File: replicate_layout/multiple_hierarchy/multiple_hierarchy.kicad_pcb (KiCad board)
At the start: 2 copper layers, 72 parts, among them J1001 Pusa_4mm, J1002 Pusa_4mm, J201 Pusa_4mm, J202 Pusa_4mm, J601 Pusa_4mm, J602 Pusa_4mm, Q1101 CSD19531KCS, Q1102 CSD19531KCS, Q1301 CSD19531KCS, Q1302 CSD19531KCS, Q1401 CSD19531KCS, Q1402 CSD19531KCS, Q301 CSD19531KCS, Q302 CSD19531KCS, Q501 CSD19531KCS, Q502 CSD19531KCS, Q701 CSD19531KCS, Q702 CSD19531KCS, Q901 CSD19531KCS, Q902 CSD19531KCS, U101 TMS320F28027DA, U1101 IR2181, U1201 INA240, U1301 IR2181, U1401 IR2181, U301 IR2181, U401 INA240, U501 IR2181, U701 IR2181, U801 INA240, U901 IR2181

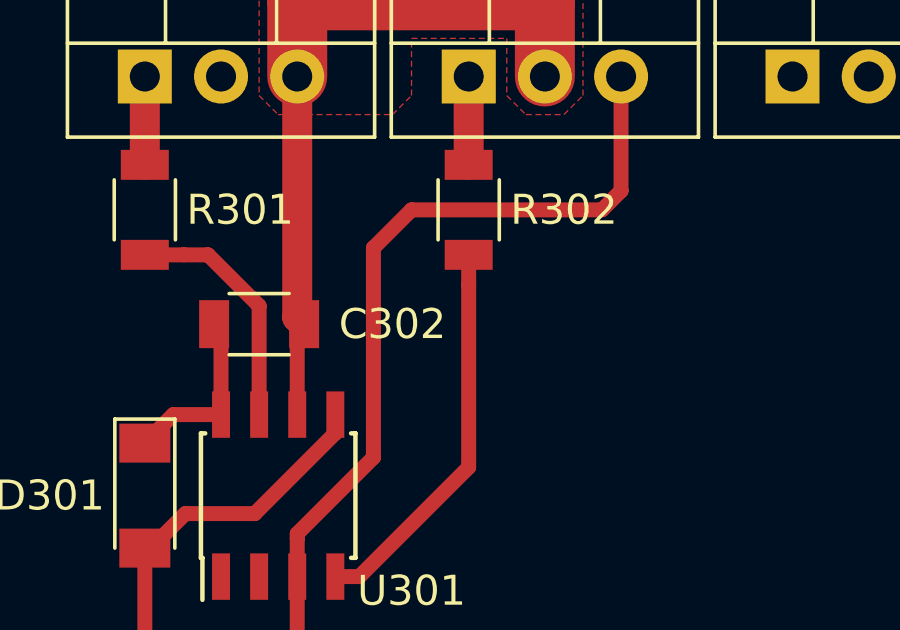
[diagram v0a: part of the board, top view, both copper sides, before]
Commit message: replicate all drawings
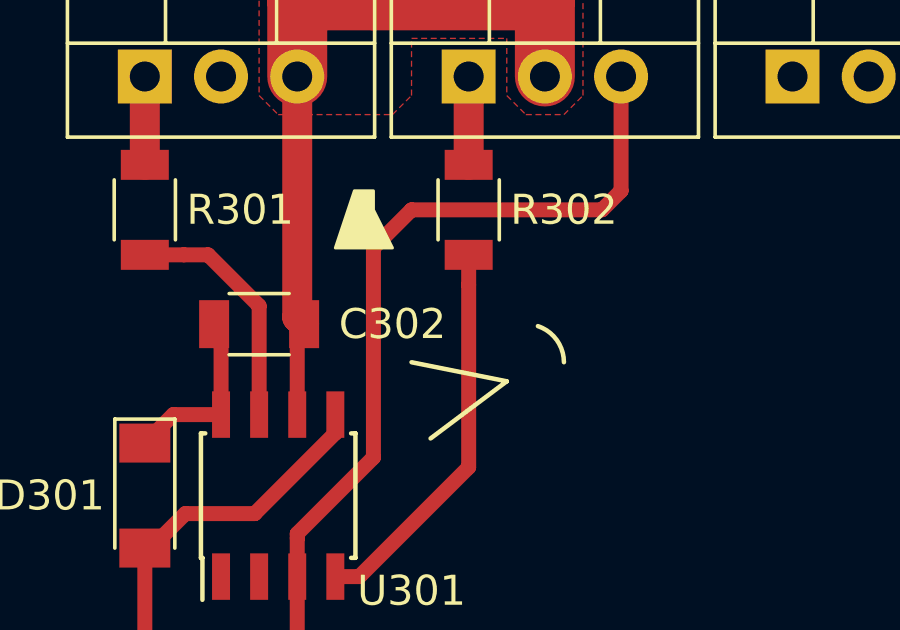
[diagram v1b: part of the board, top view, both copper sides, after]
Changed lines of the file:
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@@
-(kicad_pcb (version 20171130) (host pcbnew "(6.0.0-rc1-dev-1691-g44cb979e9)")
+(kicad_pcb (version 20171130) (host pcbnew "(5.1.0)-1")
   (general
     (thickness 1.6)
-    (drawings 1)
+    (drawings 8)
     (tracks 89)
     (zones 0)
@@
     )
   )
+  (gr_poly (pts (xy 92.71 57.15) (xy 92.075 59.055) (xy 93.98 59.055) (xy 93.345 57.785) (xy 93.345 57.15)) (layer F.SilkS) (width 0.1))
+  (gr_arc (start 98.425 62.865) (end 99.695 62.865) (angle -71.56505118) (layer F.SilkS) (width 0.15))
+  (gr_circle (center 99.695 59.055) (end 100.33 59.69) (layer F.Fab) (width 0.15))
+  (gr_line (start 97.79 63.5) (end 95.25 65.405) (layer F.SilkS) (width 0.15))
+  (gr_line (start 97.79 63.5) (end 94.615 62.865) (layer F.SilkS) (width 0.15))
+  (gr_line (start 98.425 61.595) (end 99.06 63.5) (layer F.Fab) (width 0.15))
+  (gr_line (start 94.615 63.5) (end 98.425 61.595) (layer F.Fab) (width 0.15))
   (gr_text A (at 98.425 66.675 90) (layer F.Fab)
     (effects (font (size 3 3) (thickness 0.5)))
@@
       )
     )
+  )
+  (zone (net 0) (net_name "") (layer F.Cu) (hatch edge 0.508)
+    (connect_pads (clearance 0.508))
+    (min_thickness 0.254)
+    (keepout (tracks not_allowed) (vias not_allowed) (copperpour not_allowed))
+    (fill (arc_segments 32) (thermal_gap 0.508) (thermal_bridge_width 0.508))
+    (polygon
+      (pts
+        (xy 87.63 56.515) (xy 89.535 56.515) (xy 89.535 58.42) (xy 87.63 58.42)
+      )
+    )

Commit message: Updated test projects
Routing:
- net -VDC: track 66.1 -> 66.2 mm, vias 0 -> 2
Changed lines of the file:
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@@
-(kicad_pcb (version 20171130) (host pcbnew "(5.1.0)-1")
+(kicad_pcb (version 20171130) (host pcbnew "(5.1.2)-1")
   (general
     (thickness 1.6)
     (drawings 8)
-    (tracks 89)
+    (tracks 95)
     (zones 0)
     (modules 72)
@@
   )
   (setup
-    (last_trace_width 0.25)
+    (last_trace_width 0.4)
     (user_trace_width 0.4)
     (user_trace_width 0.5)
@@
   (segment (start 90.805 68.735) (end 90.805 70.01) (width 0.5) (layer F.Cu) (net 14))
   (segment (start 90.805 68.58) (end 90.805 68.735) (width 0.5) (layer F.Cu) (net 14))
-  (segment (start 93.345 59.055) (end 93.345 66.04) (width 0.5) (layer F.Cu) (net 14))
   (segment (start 93.345 66.04) (end 90.805 68.58) (width 0.5) (layer F.Cu) (net 14))
   (segment (start 90.805 72.62) (end 90.4 73.025) (width 0.5) (layer F.Cu) (net 14))
@@
   (segment (start 186.055 54.135) (end 186.055 53.66) (width 0.5) (layer F.Cu) (net 14))
   (segment (start 186.055 53.66) (end 185.255 52.86) (width 0.5) (layer F.Cu) (net 14))
+  (via (at 93.472 65.024) (size 0.8) (drill 0.4) (layers F.Cu B.Cu) (net 14))
+  (segment (start 93.345 66.04) (end 93.345 65.151) (width 0.4) (layer F.Cu) (net 14))
+  (segment (start 93.345 65.151) (end 93.472 65.024) (width 0.4) (layer F.Cu) (net 14))
+  (segment (start 93.472 65.024) (end 93.472 60.452) (width 0.4) (layer B.Cu) (net 14))
+  (via (at 93.472 60.452) (size 0.8) (drill 0.4) (layers F.Cu B.Cu) (net 14))
+  (segment (start 93.472 59.182) (end 93.472 60.452) (width 0.4) (layer F.Cu) (net 14))
+  (segment (start 93.345 59.055) (end 93.472 59.182) (width 0.4) (layer F.Cu) (net 14))
   (segment (start 87.025 59.285) (end 85.725 59.285) (width 0.5) (layer F.Cu) (net 17))
   (segment (start 87.835002 59.285) (end 87.025 59.285) (width 0.5) (layer F.Cu) (net 17))

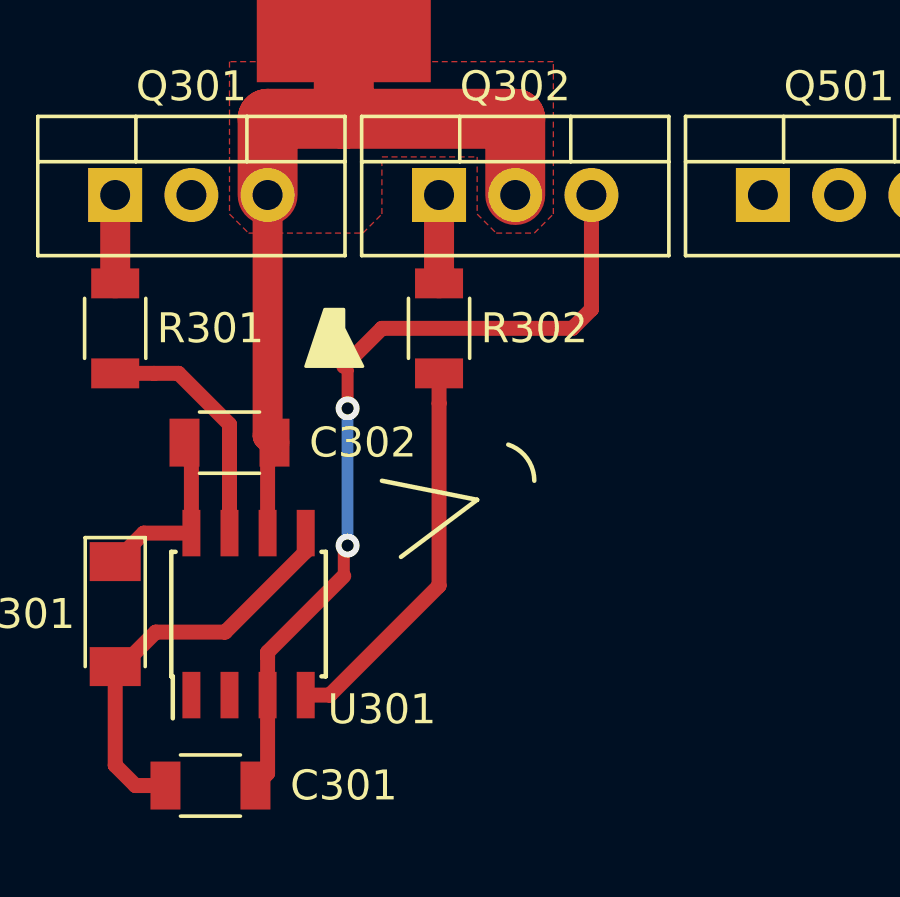
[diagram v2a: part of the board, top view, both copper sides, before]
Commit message: Modified test layouts so that one footprint is on bottom layer
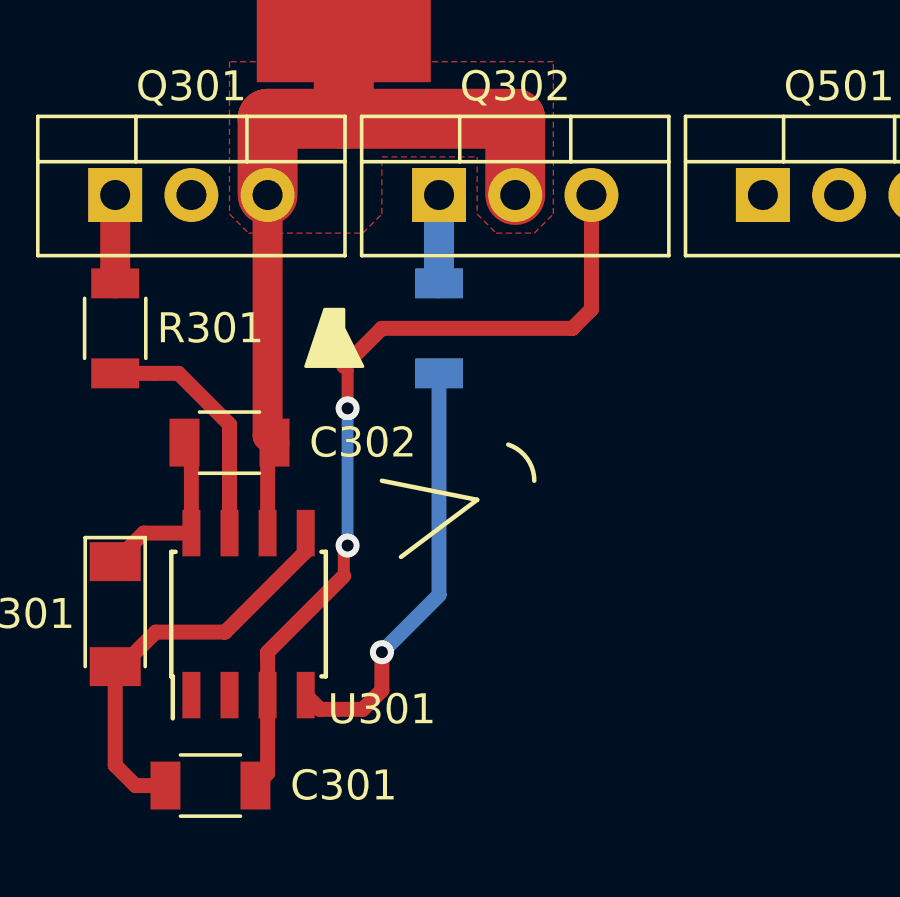
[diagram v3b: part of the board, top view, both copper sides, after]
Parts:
- R302: moved to B.Cu
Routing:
- net Net-(R302-Pad1): track 13.0 -> 14.4 mm, vias 0 -> 1
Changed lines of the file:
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@@
-(kicad_pcb (version 20171130) (host pcbnew "(5.1.2)-1")
+(kicad_pcb (version 20171130) (host pcbnew "(5.1.5-90-g5c7ac1bb7)-1")
   (general
     (thickness 1.6)
     (drawings 8)
-    (tracks 95)
+    (tracks 98)
     (zones 0)
     (modules 72)
@@
   )
   (setup
-    (last_trace_width 0.4)
+    (last_trace_width 0.5)
     (user_trace_width 0.4)
     (user_trace_width 0.5)
@@
     )
   )
-  (module Passives:R1206M (layer F.Cu)
+  (module Passives:R1206M (layer B.Cu)
     (at 96.52 57.785 90)
     (descr "Capacitor SMD 1206, reflow soldering, AVX (see smccp.pdf)")
     (tags "capacitor 1206")
     (attr smd)
-    (fp_text reference R302 (at 0 3.175 180) (layer F.SilkS)
-      (effects (font (size 1 1) (thickness 0.15)))
+    (fp_text reference R302 (at 0 -3.175 180) (layer B.SilkS)
+      (effects (font (size 1 1) (thickness 0.15)) (justify mirror))
     )
-    (fp_text value 22R (at 0 2 90) (layer F.Fab) hide
-      (effects (font (size 1 1) (thickness 0.15)))
+    (fp_text value 22R (at 0 -2 270) (layer B.Fab) hide
+      (effects (font (size 1 1) (thickness 0.15)) (justify mirror))
     )
-    (fp_line (start 2.25 1.05) (end -2.25 1.05) (layer F.CrtYd) (width 0.05))
-    (fp_line (start 2.25 1.05) (end 2.25 -1.05) (layer F.CrtYd) (width 0.05))
-    (fp_line (start -2.25 -1.05) (end -2.25 1.05) (layer F.CrtYd) (width 0.05))
-    (fp_line (start -2.25 -1.05) (end 2.25 -1.05) (layer F.CrtYd) (width 0.05))
-    (fp_line (start -1 1.02) (end 1 1.02) (layer F.SilkS) (width 0.12))
-    (fp_line (start 1 -1.02) (end -1 -1.02) (layer F.SilkS) (width 0.12))
-    (fp_line (start -1.6 -0.8) (end 1.6 -0.8) (layer F.Fab) (width 0.1))
-    (fp_line (start 1.6 -0.8) (end 1.6 0.8) (layer F.Fab) (width 0.1))
-    (fp_line (start 1.6 0.8) (end -1.6 0.8) (layer F.Fab) (width 0.1))
-    (fp_line (start -1.6 0.8) (end -1.6 -0.8) (layer F.Fab) (width 0.1))
-    (fp_text user %R (at 0 0 90) (layer F.Fab)
-      (effects (font (size 0.5 0.5) (thickness 0.07)))
+    (fp_line (start 2.25 -1.05) (end -2.25 -1.05) (layer B.CrtYd) (width 0.05))
+    (fp_line (start 2.25 -1.05) (end 2.25 1.05) (layer B.CrtYd) (width 0.05))
+    (fp_line (start -2.25 1.05) (end -2.25 -1.05) (layer B.CrtYd) (width 0.05))
+    (fp_line (start -2.25 1.05) (end 2.25 1.05) (layer B.CrtYd) (width 0.05))
+    (fp_line (start -1 -1.02) (end 1 -1.02) (layer B.SilkS) (width 0.12))
+    (fp_line (start 1 1.02) (end -1 1.02) (layer B.SilkS) (width 0.12))
+    (fp_line (start -1.6 0.8) (end 1.6 0.8) (layer B.Fab) (width 0.1))
+    (fp_line (start 1.6 0.8) (end 1.6 -0.8) (layer B.Fab) (width 0.1))
+    (fp_line (start 1.6 -0.8) (end -1.6 -0.8) (layer B.Fab) (width 0.1))
+    (fp_line (start -1.6 -0.8) (end -1.6 0.8) (layer B.Fab) (width 0.1))
+    (fp_text user %R (at 0 0 270) (layer B.Fab)
+      (effects (font (size 0.5 0.5) (thickness 0.07)) (justify mirror))
     )
-    (pad 2 smd rect (at 1.5 0 90) (size 1 1.6) (layers F.Cu F.Paste F.Mask)
+    (pad 2 smd rect (at 1.5 0 90) (size 1 1.6) (layers B.Cu B.Paste B.Mask)
       (net 13 "Net-(Q302-Pad1)"))
-    (pad 1 smd rect (at -1.5 0 90) (size 1 1.6) (layers F.Cu F.Paste F.Mask)
+    (pad 1 smd rect (at -1.5 0 90) (size 1 1.6) (layers B.Cu B.Paste B.Mask)
       (net 18 "Net-(R302-Pad1)"))
     (model ${KISYS3DMOD}/Resistor_SMD.3dshapes/R_1206_3216Metric.wrl
@@
   (segment (start 93.345 28.575) (end 93.345 38.18) (width 2) (layer F.Cu) (net 8))
   (segment (start 85.725 53.34) (end 85.725 56.285) (width 1) (layer F.Cu) (net 12))
-  (segment (start 96.52 53.34) (end 96.52 56.285) (width 1) (layer F.Cu) (net 13))
+  (segment (start 96.52 56.285) (end 96.52 53.34) (width 1) (layer B.Cu) (net 13))
   (segment (start 86.77 40.82) (end 85.32 39.37) (width 0.4) (layer F.Cu) (net 14))
   (segment (start 86.77 41.57) (end 86.77 40.82) (width 0.4) (layer F.Cu) (net 14))
@@
   (segment (start 89.535 64.61) (end 89.535 60.984998) (width 0.5) (layer F.Cu) (net 17))
   (segment (start 89.535 60.984998) (end 87.835002 59.285) (width 0.5) (layer F.Cu) (net 17))
-  (segment (start 96.52 60.285) (end 96.52 59.285) (width 0.5) (layer F.Cu) (net 18))
-  (segment (start 96.52 66.365) (end 96.52 60.285) (width 0.5) (layer F.Cu) (net 18))
-  (segment (start 92.075 70.01) (end 92.875 70.01) (width 0.5) (layer F.Cu) (net 18))
-  (segment (start 92.875 70.01) (end 96.52 66.365) (width 0.5) (layer F.Cu) (net 18))
+  (segment (start 96.52 59.285) (end 96.52 66.675) (width 0.5) (layer B.Cu) (net 18))
+  (via (at 94.615 68.58) (size 0.8) (drill 0.4) (layers F.Cu B.Cu) (net 18))
+  (segment (start 96.52 66.675) (end 94.615 68.58) (width 0.5) (layer B.Cu) (net 18))
+  (segment (start 94.615 68.58) (end 94.615 69.85) (width 0.5) (layer F.Cu) (net 18))
+  (segment (start 94.615 69.85) (end 93.98 70.485) (width 0.5) (layer F.Cu) (net 18))
+  (segment (start 92.55 70.485) (end 92.075 70.01) (width 0.5) (layer F.Cu) (net 18))
+  (segment (start 93.98 70.485) (end 92.55 70.485) (width 0.5) (layer F.Cu) (net 18))
   (segment (start 97.485 42.22) (end 97.545 42.28) (width 0.4) (layer F.Cu) (net 19))
   (segment (start 86.77 42.22) (end 97.485 42.22) (width 0.4) (layer F.Cu) (net 19))

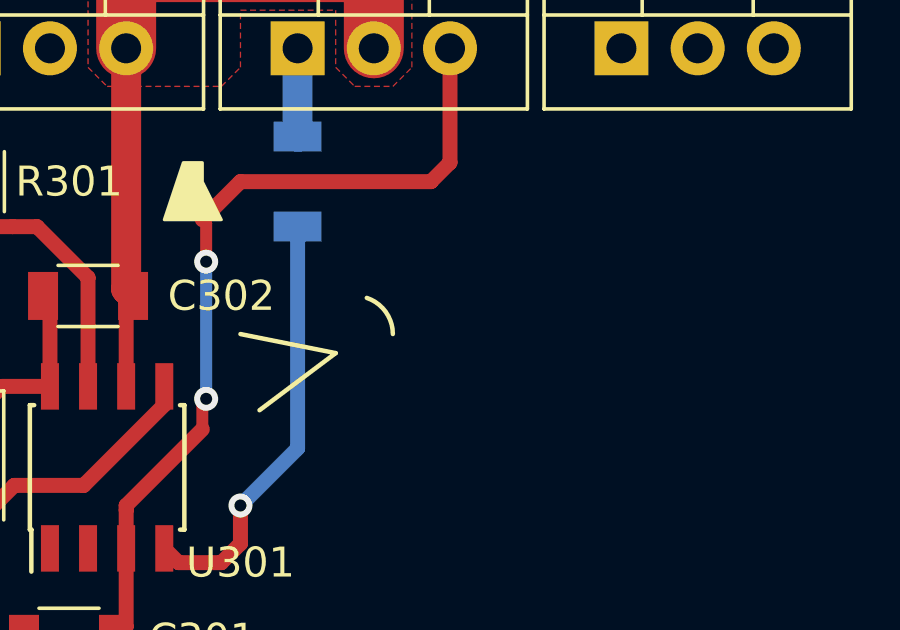
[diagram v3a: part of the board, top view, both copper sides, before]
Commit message: Add the option to replicate edge cuts items only when required
Fixes: #117
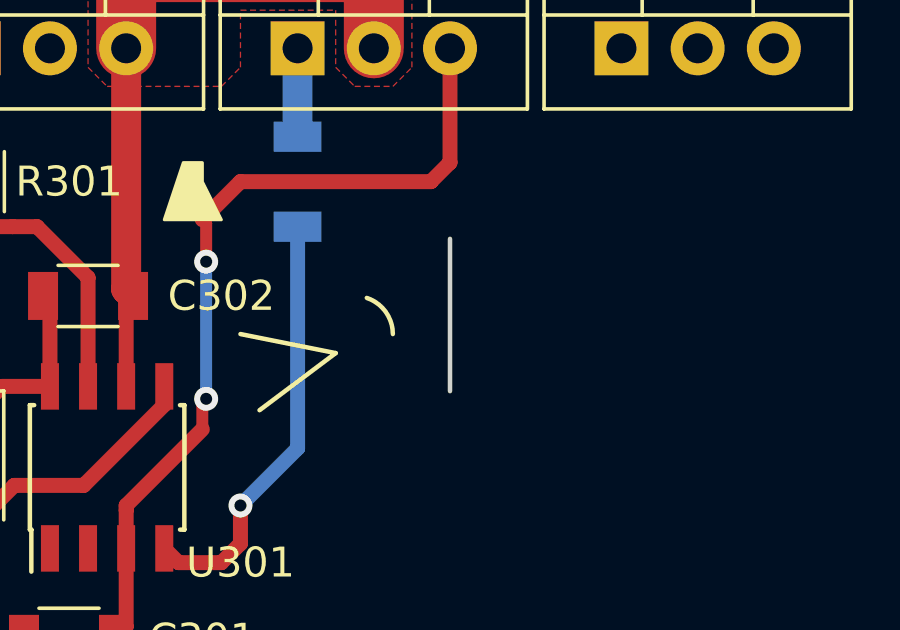
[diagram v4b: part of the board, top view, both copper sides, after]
